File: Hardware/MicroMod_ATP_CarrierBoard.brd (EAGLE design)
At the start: 101.6 x 58.4 mm, 144 parts, among them J12 SPI, J15 Dedicated, J2 JTAG, J4 USB_A_SMT_FEMALE, J6 MICROMOD-2222-C, J8 Dedicated, U5 AP7361C-33

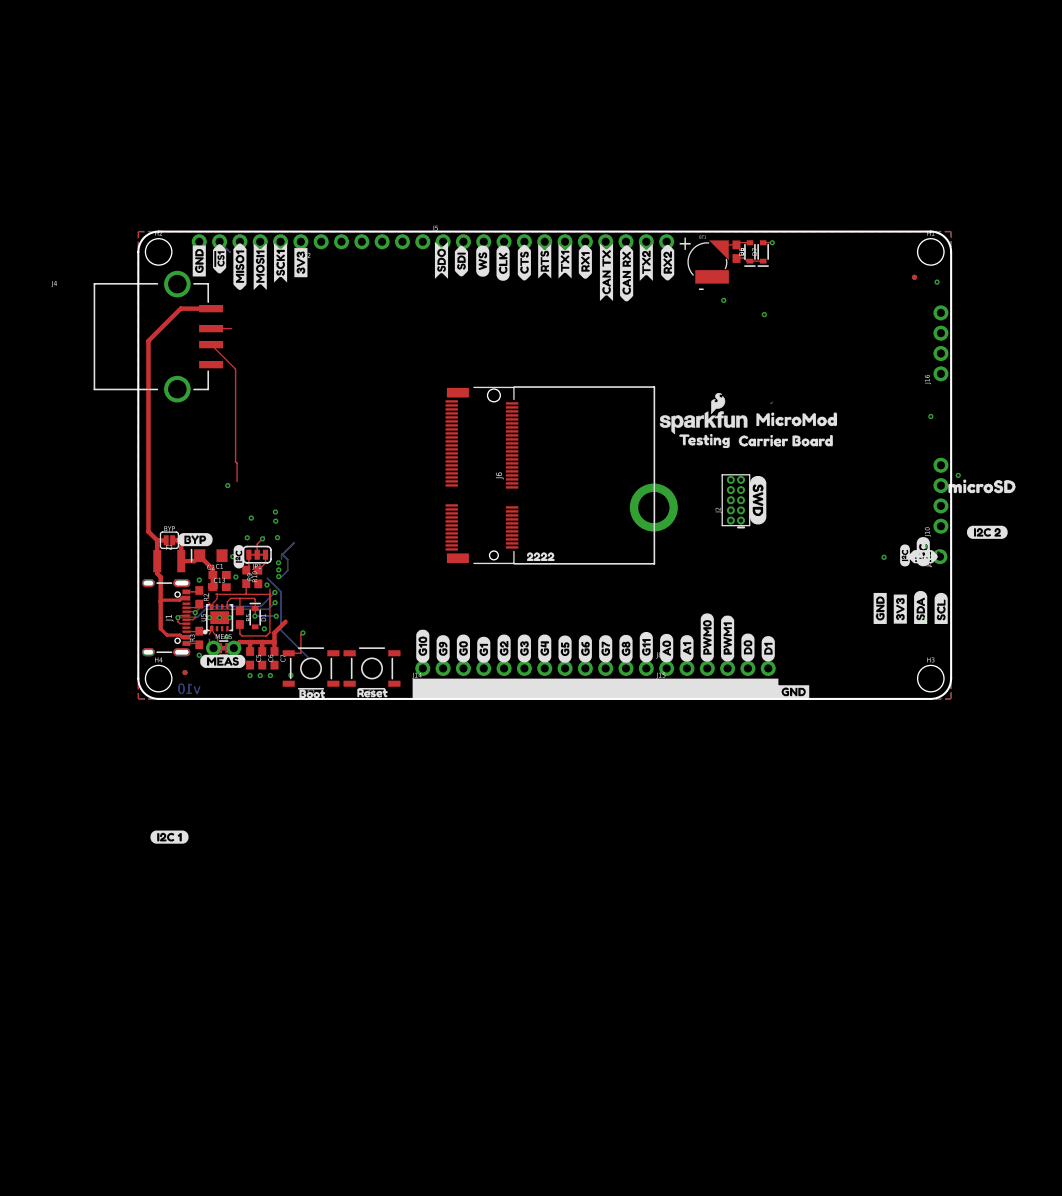
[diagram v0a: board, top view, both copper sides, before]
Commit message: Many headers added, netted, and placed into form factor
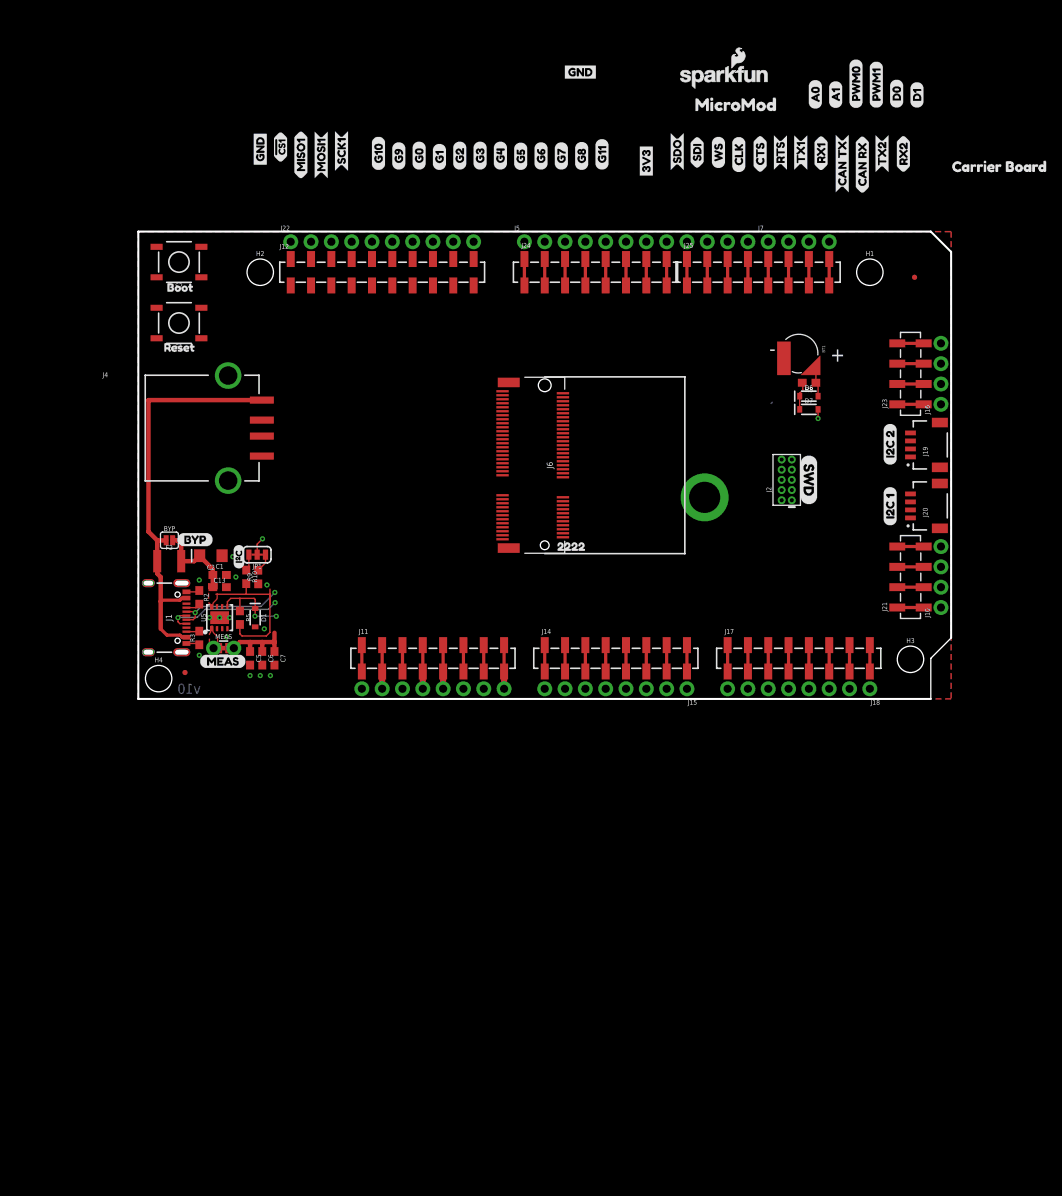
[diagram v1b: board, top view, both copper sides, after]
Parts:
- removed J8: Dedicated, SparkFun-Connectors:1X06_NO_SILK
- removed J9: (no value), SparkFun-Connectors:1X01_NO_SILK
- removed U$100: (no value), Labels:GND-04
- removed U$101: (no value), Labels:I_SUPER2_C-()-03
- removed U$21, U$35: (no value), SparkFun-Buzzard:!INT_I
- removed U$28: (no value), buzzard_labels (10):MICROSD4
- removed U$46: (no value), testing:TESTING0
- removed U$64: (no value), buzzard_labels (11):MICROMOD0
- removed U$96: (no value), Labels:SCL-[)
- removed U$97: (no value), Labels:SDA-[)
- removed U$98: (no value), Labels:I_SUPER2_C-()-04
- removed U$99: (no value), Labels:3V3-04
- added J11, J17, J24, J25: (no value), SparkFun-Connectors:1X08_SMD_COMBINED
- added J13, J18: (no value), SparkFun-Connectors:1X08_NO_SILK
- added J19, J20: QWIIC_RIGHT_ANGLE, SparkFun-Connectors:JST04_1MM_RA
- added J21, J23: 1X04_SMD_STRAIGHT_COMBO, SparkFun-Connectors:1X04_SMD_VERTICAL_COMBO
- added J22: (no value), SparkFun-Connectors:1X04_NO_SILK
- J12: value SPI -> (none); device SparkFun-Connectors:1X06_NO_SILK -> SparkFun-Connectors:1X10_SMD_COMBINED
- J14: device SparkFun-Connectors:1X12_NO_SILK -> SparkFun-Connectors:1X08_SMD_COMBINED
- J15: value Dedicated -> (none); device SparkFun-Connectors:1X06_NO_SILK -> SparkFun-Connectors:1X08_NO_SILK
- J7: device SparkFun-Connectors:1X12_NO_SILK -> SparkFun-Connectors:1X04_NO_SILK
- moved U$67 100.4 mm to (94.0, 21.6), turned to 90 degrees
- moved U$73 81.9 mm to (52.8, 78.4)
- moved U$12 71.7 mm to (97.3, 73.8)
- moved U$13 71.7 mm to (97.3, 73.8)
- moved U$14 71.7 mm to (94.8, 73.8)
- moved U$15 71.7 mm to (92.2, 73.8)
- moved U$16 71.7 mm to (94.8, 73.8)
- moved U$57 71.7 mm to (87.2, 73.8)
- moved U$58 71.7 mm to (87.2, 73.8)
- moved U$59 71.7 mm to (89.7, 73.8)
- moved U$60 71.7 mm to (89.7, 73.8)
- moved U$61 71.7 mm to (92.2, 73.8)
- moved U$43 71.7 mm to (84.6, 73.7)
- moved U$44 71.7 mm to (84.6, 73.7)
- moved U$1 61.9 mm to (35.1, 66.1)
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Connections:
- removed net !RESET!: J2.10, J6.6, S1.3, S1.4
- new net !RESET: J11.3, J11.3@2, J13.6, J2.10, J6.6, S1.3, S1.4
- new net 5V: J11.4, J11.4@2, J13.5
- new net VDD: J11.2, J11.2@2, J11.5, J11.5@2, J13.4, J13.7
- net !CS1: now also J12.4A, J12.4B, J22.4; no longer J12.5
- net 3.3V: now also J19.3, J20.3, J21.3, J21.3-2, J23.3, J23.3-2; no longer J12.1
- net A0: now also J14.1, J14.1@2, J15.8; no longer J8.1
- net A1: now also J14.2, J14.2@2, J15.7; no longer J8.2
- net CAN_RXI: now also J25.2, J25.2@2
- net CAN_TXO: now also J25.1, J25.1@2
- net CTS1: now also J24.5, J24.5@2
- net D0: now also J25.6, J25.6@2, J7.2; no longer J8.5
- net D1: now also J25.7, J25.7@2, J7.3; no longer J8.6
- net G0: now also J17.1, J17.1@2, J18.8; no longer J7.10
- net G1: now also J17.2, J17.2@2, J18.7; no longer J7.9
- net G10/ADC_P: now also J14.5, J14.5@2, J15.4; no longer J7.12
- net G11: now also J14.8, J14.8@2, J15.1; no longer J7.1
- net G2: now also J17.3, J17.3@2, J18.6; no longer J7.8
- net G3: now also J17.4, J17.4@2, J18.5; no longer J7.7
- net G4: now also J17.5, J17.5@2, J18.4; no longer J7.6
- net G5: now also J17.6, J17.6@2, J18.3; no longer J7.5
- net G6: now also J17.7, J17.7@2, J18.2; no longer J7.4
- net G7: now also J17.8, J17.8@2, J18.1; no longer J7.3
- net G8: now also J14.7, J14.7@2, J15.2; no longer J7.2
- net G9/ADC_N: now also J14.6, J14.6@2, J15.3; no longer J7.11
- net GND: now also J11.6, J11.6@2, J11.7, J11.7@2, J13.2, J13.3, J19.4, J20.4, J21.4, J21.4-2, J23.4, J23.4-2, J25.8, J25.8@2, J7.4; no longer J12.6, J14.1, J14.10, J14.11, J14.12, J14.2, J14.3, J14.4, J14.5, J14.6, J14.7, J14.8, J14.9, J15.1, J15.2, J15.3, J15.4, J15.5, J15.6
- net I2C_!INT: now also J25.5, J25.5@2, J7.1; no longer J9.1
- net I2S_CLK: now also J24.4, J24.4@2
- net I2S_SDI: now also J24.2, J24.2@2
- net I2S_SDO: now also J24.1, J24.1@2
- net I2S_WS: now also J24.3, J24.3@2
- net MISO1: now also J12.3A, J12.3B, J22.3; no longer J12.4
- net MOSI1: now also J12.2A, J12.2B, J22.2; no longer J12.3
- net PWM0: now also J14.3, J14.3@2, J15.6; no longer J8.3
- net PWM1: now also J14.4, J14.4@2, J15.5; no longer J8.4
- net RTS1: now also J24.6, J24.6@2
- net RX1: now also J24.8, J24.8@2
- net RX2: now also J25.4, J25.4@2
- net SCL: now also J20.1, J23.1, J23.1-2
- net SCL1: now also J19.1, J21.1, J21.1-2
- net SCLK1: now also J12.1A, J12.1B, J22.1; no longer J12.2
- net SDA: now also J20.2, J23.2, J23.2-2
- net SDA1: now also J19.2, J21.2, J21.2-2
- net SD_!CS!: now also J12.5A, J12.5B
- net SD_DAT1: now also J12.7A, J12.7B
- net SD_DAT2: now also J12.6A, J12.6B
- net SPI_MISO: now also J12.8A, J12.8B
- net SPI_MOSI: now also J12.10A, J12.10B
- net SPI_SCK: now also J12.9A, J12.9B
- net TX1: now also J24.7, J24.7@2
- net TX2: now also J25.3, J25.3@2
- net VIN: now also J11.8, J11.8@2, J13.1
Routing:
- net USBHOST_P: track 18.4 -> 0.00 mm
- net G6: track 12.0 -> 0.00 mm
- net RTS1: track 6.55 -> 0.00 mm, vias 1 -> 0
- net !BOOT!: track 4.17 -> 0.00 mm, vias 1 -> 0
- net VDD: track 0.00 -> 3.56 mm
- net V_USB: track 54.3 -> 51.6 mm
- net USBHOST_N: track 2.54 -> 0.00 mm
- net 3.3V: track 14.2 -> 12.2 mm
- net !CS1: track 1.87 -> 0.00 mm
- net 5V: track 0.00 -> 1.78 mm
- net VIN: track 30.6 -> 32.4 mm
- net I2C_!INT: track 1.62 -> 0.00 mm
- net A0: track 0.32 -> 0.00 mm, vias 1 -> 0
- net GND: vias 29 -> 13
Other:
- outline, holes or cut-outs redrawn

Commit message: Trace work for ATP board
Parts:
- added D2: RED, SparkFun-LED:LED-0603
- added J8: 1X04_SMD_STRAIGHT_COMBO, SparkFun-Connectors:1X04_NO_SILK
- added JP2: JUMPER-SMT_2_NC_TRACE_SILK, SparkFun-Jumpers:SMT-JUMPER_2_NC_TRACE_SILK
- added R1: 1k, SparkFun-Resistors:0603
- moved R3 38.1 mm to (7.62, 45.7)
- moved J1 38.1 mm to (6.35, 48.3)
- moved R2 38.1 mm to (7.62, 50.8)
- moved S1 37.8 mm to (30.5, 19.1), turned to 0 degrees
- moved S2 36.5 mm to (29.2, 27.2)
- moved J21 25.4 mm to (96.5, 36.8)
- moved J23 25.4 mm to (96.5, 11.4)
- moved U$42 7.70 mm to (17.3, 22.4), turned to 0 degrees
- moved C2 4.98 mm to (13.0, 21.0)
- moved R10 4.97 mm to (17.7, 17.9)
- moved R9 4.97 mm to (19.2, 17.9)
- moved JP1 4.58 mm to (18.7, 20.6)
- moved R5 4.58 mm to (16.5, 12.7)
- moved C13 4.58 mm to (14.0, 16.5)
- moved C5 4.58 mm to (17.8, 7.62)
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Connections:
- net G10/ADC_P renamed ADC_P
- net G9/ADC_N renamed ADC_N
- new net N$1: D2.A, R1.1
- new net N$4: D2.C, JP2.2
- net !CS1: now also J12.1A, J12.1B, J22.1; no longer J12.4A, J12.4B, J22.4
- net 3.3V: now also R1.2
- net GND: now also J8.1, JP2.1
- net MISO1: now also J12.4A, J12.4B, J22.4; no longer J12.3A, J12.3B, J22.3
- net MOSI1: now also J12.3A, J12.3B, J22.3; no longer J12.2A, J12.2B, J22.2
- net SCLK1: now also J12.2A, J12.2B, J22.2; no longer J12.1A, J12.1B, J22.1
- net SPI_MOSI: now also J12.9A, J12.9B, J3.5; no longer J12.10A, J12.10B, J3.6
- net SPI_SCK: now also J12.10A, J12.10B, J3.6; no longer J12.9A, J12.9B, J3.5
- net USBHOST_N: now also J8.3
- net USBHOST_P: now also J8.2
- net V_USB: now also J8.4
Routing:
- net V_USB: track 51.6 -> 5.26 mm
- net SD_!CS!: track 0.00 -> 45.9 mm
- net ADC_N: track 0.00 -> 43.7 mm
- net ADC_P: track 0.00 -> 43.0 mm
- net SD_DAT2: track 0.00 -> 42.5 mm
- net SD_DAT1: track 0.00 -> 41.8 mm
- net SPI_MISO: track 0.00 -> 40.6 mm
- net !CS1: track 0.00 -> 40.1 mm
- net SPI_SCK: track 0.00 -> 39.6 mm
- net SPI_MOSI: track 0.00 -> 39.2 mm
- net SCLK1: track 0.00 -> 38.5 mm
- net MOSI1: track 0.00 -> 37.0 mm
- net MISO1: track 0.00 -> 35.3 mm
- net USB_P: track 15.7 -> 0.00 mm, vias 2 -> 0
- net USB_N: track 14.0 -> 0.00 mm, vias 2 -> 0
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
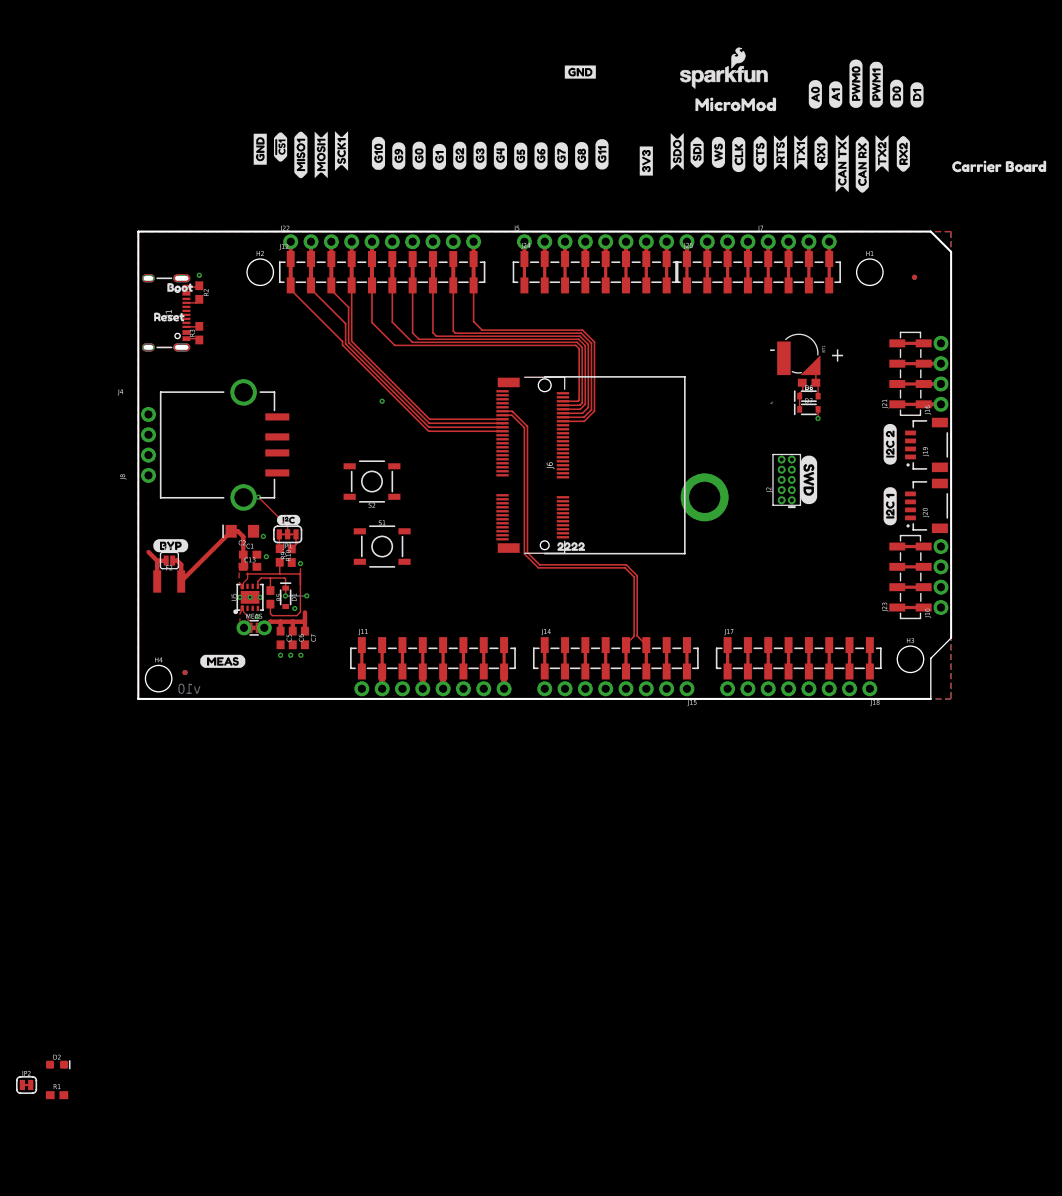
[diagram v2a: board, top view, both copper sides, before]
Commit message: Adds barrel jack for power
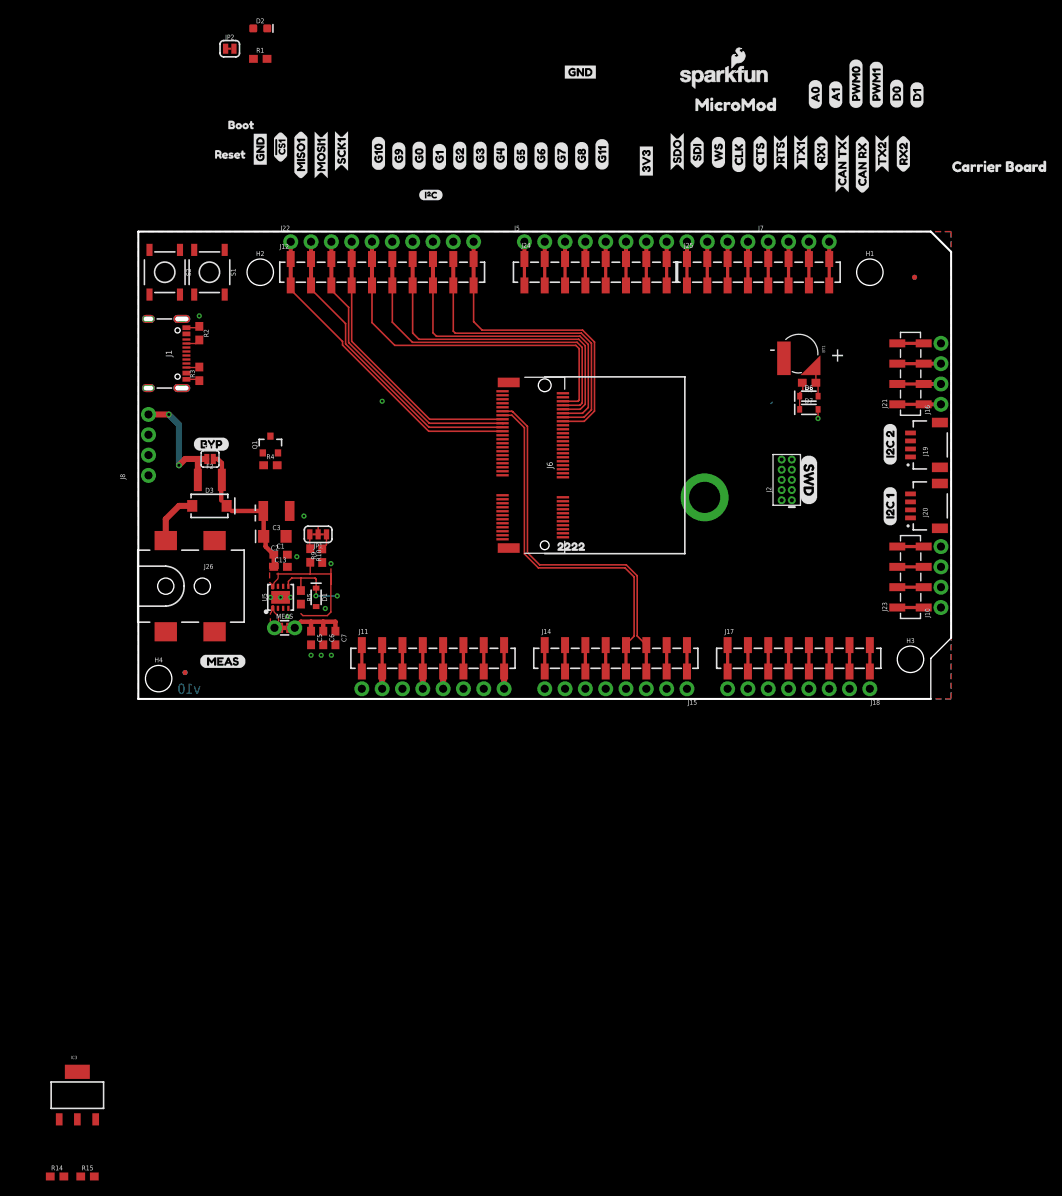
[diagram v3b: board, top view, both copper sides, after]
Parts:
- removed J4: USB_A_SMT_FEMALE, SparkFun-Connectors:USB-A-S-SILK-FEMALE
- added C3: 47uF, SparkFun-Capacitors:EIA3528
- added D3: 1A/40V/500mV, SparkFun-DiscreteSemi:SMA-DIODE
- added IC3: LM1117, Testing:SOT223-ALT1
- added J26: POWER_JACKTOE, SparkFun-Connectors:POWER_JACK_SMD_OVERPASTE_TOE
- added Q1: 2.5A/30V/105mΩ, SparkFun-DiscreteSemi:SOT23-3
- added R14: 715, SparkFun-Resistors:0603
- added R15: 240, SparkFun-Resistors:0603
- added R4: 10k, SparkFun-Resistors:0603
- D1: device SparkFun-DiscreteSemi:SOD-323 -> SparkFun-DiscreteSemi:SOD-323@1
- moved R1 132.0 mm to (15.2, 80.0)
- moved D2 132.0 mm to (15.2, 83.8)
- moved JP2 132.0 mm to (11.4, 81.3)
- moved U$42 44.4 mm to (35.1, 63.0)
- moved S1 40.5 mm to (8.89, 53.3), turned to 270 degrees
- moved S2 36.8 mm to (3.30, 53.3), turned to 270 degrees
- moved U$2 21.7 mm to (8.64, 68.1)
- moved U$19 21.7 mm to (10.3, 71.8)
- moved U$27 13.7 mm to (6.83, 31.9)
- moved BYP 13.7 mm to (8.97, 30.0)
- moved F2 13.7 mm to (8.94, 27.4)
- moved J1 5.08 mm to (6.35, 43.2)
- moved R2 5.08 mm to (7.62, 45.7)
- moved R3 5.08 mm to (7.62, 40.6)
- moved C2 4.11 mm to (17.1, 20.3)
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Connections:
- new net INSERT: J26.P$4, Q1.1, R4.1
- new net N$15: IC3.1, R14.2, R15.1
- new net PWRIN: D3.A, J26.VIN0
- new net SHIELD: J1.SHLD1, J1.SHLD2, J1.SHLD3, J1.SHLD4
- net 5V: now also C1.1, C13.1, C2.+, IC3.2, IC3.4, Q1.2, R15.2, R4.2, R5.2, U5.8
- net GND: now also C3.C, J26.GND, R14.1; no longer J4.GND, J4.SHLD1, J4.SHLD2
- net USBHOST_N: no longer J4.D-
- net USBHOST_P: no longer J4.D+
- net VIN: now also C3.A, D3.C, IC3.3; no longer C1.1, C13.1, C2.+, R5.2, U5.8
- net V_USB: now also Q1.3; no longer J4.VBUS
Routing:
- net V_USB: track 5.26 -> 15.9 mm, vias 0 -> 2
- net VIN: track 39.7 -> 30.9 mm
- net 5V: track 1.78 -> 9.38 mm
- net PWRIN: track 0.00 -> 6.68 mm
- net VIN/3: track 6.16 -> 0.99 mm, vias 1 -> 0
- net 3.3V: track 14.4 -> 13.2 mm
